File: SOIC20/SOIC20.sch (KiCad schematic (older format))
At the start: 5 parts, among them J1 Conn_01x10, J2 Conn_02x10_Counter_Clockwise, J3 Conn_02x10_Counter_Clockwise, J4 Conn_02x10_Counter_Clockwise, J5 Conn_01x10

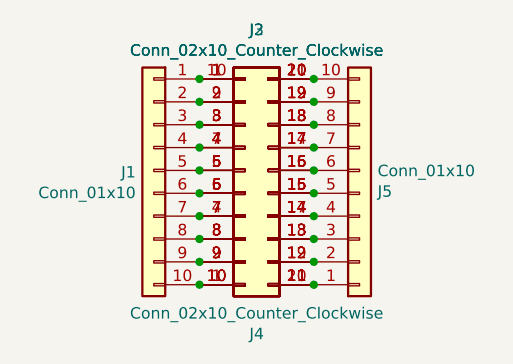
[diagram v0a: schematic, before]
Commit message: Silkscreens and sizes updated
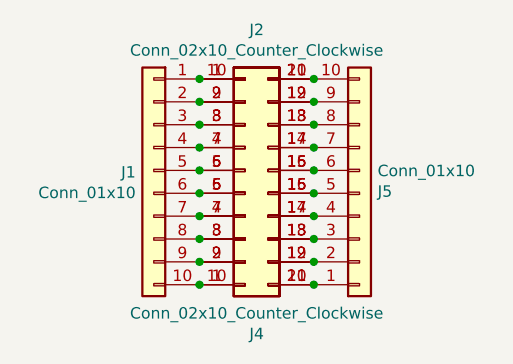
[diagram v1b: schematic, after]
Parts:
- removed J3: Conn_02x10_Counter_Clockwise, Package_DFN_QFN:QFN-20-1EP_5x5mm_P0.65mm_EP3.35x3.35mm, symbol Connector_Generic:Conn_02x10_Counter_Clockwise
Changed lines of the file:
@@
 EESchema Schematic File Version 4
+LIBS:SOIC20-cache
 EELAYER 29 0
 EELAYER END
@@
 	1    0    0    1
 $EndComp
-$Comp
-L Connector_Generic:Conn_02x10_Counter_Clockwise J3
-U 1 1 5D28B720
-P 4600 3700
-F 0 "J3" H 4650 4315 50  0000 C CNN
-F 1 "Conn_02x10_Counter_Clockwise" H 4650 4225 50  0000 C CNN
-F 2 "Package_DFN_QFN:QFN-20-1EP_5x5mm_P0.65mm_EP3.35x3.35mm" H 4600 3700 50  0001 C CNN
-F 3 "~" H 4600 3700 50  0001 C CNN
-	1    4600 3700
-	1    0    0    -1
-$EndComp
 Connection ~ 4400 3300

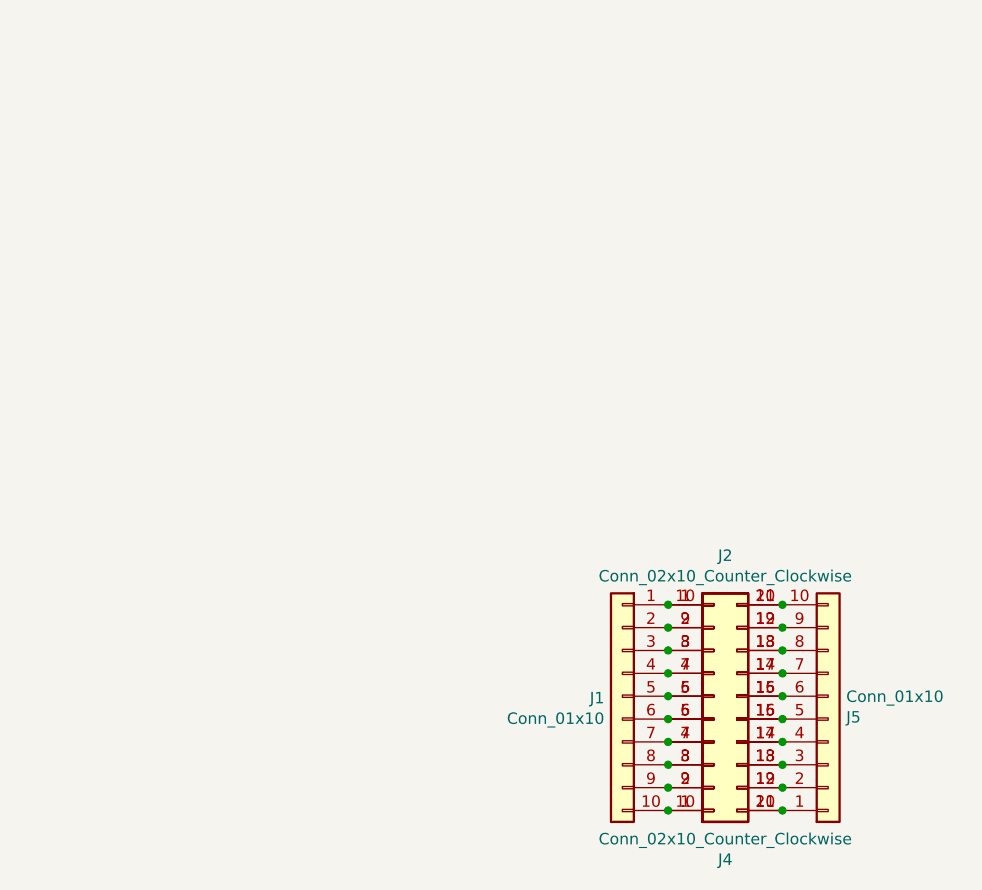
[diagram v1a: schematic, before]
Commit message: USB, SD and CR Cells Added
MicroSD, MicroUSB, MiniUSB, USB-C, CR1220, CR2032 added as well as all schematics page sizes optimised
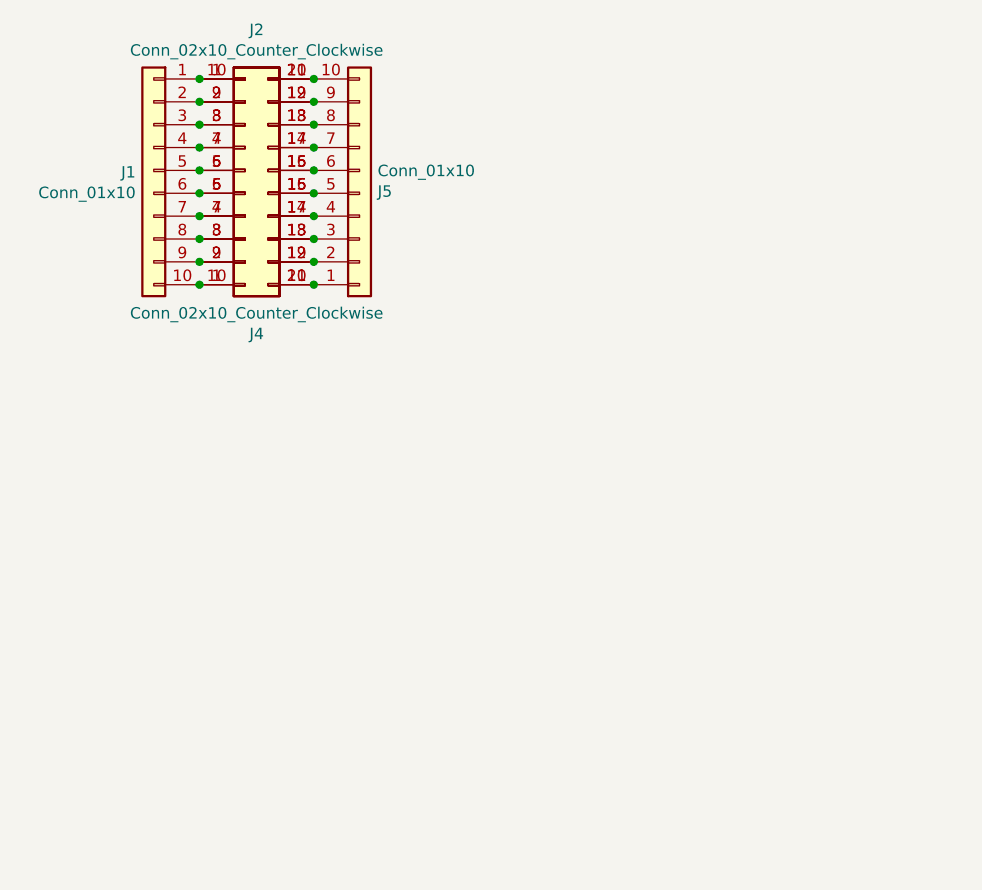
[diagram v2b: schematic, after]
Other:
- moved on the sheet: J1, J2, J4, J5
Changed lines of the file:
@@
 EELAYER 29 0
 EELAYER END
-$Descr A4 11693 8268
+$Descr User 5197 4016
 encoding utf-8
 Sheet 1 1
-Title ""
-Date ""
-Rev ""
-Comp ""
-Comment1 ""
-Comment2 ""
-Comment3 ""
+Title "SOIC20 To DIP20 Breakout Board"
+Date "2019-07-10"
+Rev "1"
+Comp "SirBoard"
+Comment1 "SOIC20 P = 1.27mm"
+Comment2 "TSSOP20 P = 0.65mm"
+Comment3 "DIP20 P = 2.54mm"
 Comment4 ""
 $EndDescr
@@
 L Connector_Generic:Conn_01x10 J5
 U 1 1 5D259BCE
-P 5100 3800
-F 0 "J5" H 5179 3792 50  0000 L CNN
-F 1 "Conn_01x10" H 5179 3702 50  0000 L CNN
-F 2 "Connector_PinHeader_2.54mm:PinHeader_1x10_P2.54mm_Vertical" H 5100 3800 50  0001 C CNN
-F 3 "~" H 5100 3800 50  0001 C CNN
-	1    5100 3800
+P 3050 1500
+F 0 "J5" H 3129 1492 50  0000 L CNN
+F 1 "Conn_01x10" H 3129 1402 50  0000 L CNN
+F 2 "Connector_PinHeader_2.54mm:PinHeader_1x10_P2.54mm_Vertical" H 3050 1500 50  0001 C CNN
+F 3 "~" H 3050 1500 50  0001 C CNN
+	1    3050 1500
 	1    0    0    1
 $EndComp
@@
 L Connector_Generic:Conn_01x10 J1
 U 1 1 5D25B9B9
-P 4200 3700
-F 0 "J1" H 4279 3692 50  0000 L CNN
-F 1 "Conn_01x10" H 4279 3602 50  0000 L CNN
-F 2 "Connector_PinHeader_2.54mm:PinHeader_1x10_P2.54mm_Vertical" H 4200 3700 50  0001 C CNN
-F 3 "~" H 4200 3700 50  0001 C CNN
-	1    4200 3700
+P 2150 1400
+F 0 "J1" H 2229 1392 50  0000 L CNN
+F 1 "Conn_01x10" H 2229 1302 50  0000 L CNN
+F 2 "Connector_PinHeader_2.54mm:PinHeader_1x10_P2.54mm_Vertical" H 2150 1400 50  0001 C CNN
+F 3 "~" H 2150 1400 50  0001 C CNN
+	1    2150 1400
 	-1   0    0    -1
 $EndComp
@@
 L Connector_Generic:Conn_02x10_Counter_Clockwise J2
 U 1 1 5D25A016
-P 4600 3700
-F 0 "J2" H 4650 4315 50  0000 C CNN
-F 1 "Conn_02x10_Counter_Clockwise" H 4650 4225 50  0000 C CNN
-F 2 "Package_SO:SOIC-20W_7.5x12.8mm_P1.27mm" H 4600 3700 50  0001 C CNN
-F 3 "~" H 4600 3700 50  0001 C CNN
-	1    4600 3700
+P 2550 1400
+F 0 "J2" H 2600 2015 50  0000 C CNN
+F 1 "Conn_02x10_Counter_Clockwise" H 2600 1925 50  0000 C CNN
+F 2 "Package_SO:SOIC-20W_7.5x12.8mm_P1.27mm" H 2550 1400 50  0001 C CNN
+F 3 "~" H 2550 1400 50  0001 C CNN
+	1    2550 1400
 	1    0    0    -1
 $EndComp
@@
 L Connector_Generic:Conn_02x10_Counter_Clockwise J4
 U 1 1 5D25E8E3
-P 4600 3800
-F 0 "J4" H 4650 4415 50  0000 C CNN
-F 1 "Conn_02x10_Counter_Clockwise" H 4650 4325 50  0000 C CNN
-F 2 "Package_SO:SSOP-20_4.4x6.5mm_P0.65mm" H 4600 3800 50  0001 C CNN
-F 3 "~" H 4600 3800 50  0001 C CNN
-	1    4600 3800
+P 2550 1500
+F 0 "J4" H 2600 2115 50  0000 C CNN
+F 1 "Conn_02x10_Counter_Clockwise" H 2600 2025 50  0000 C CNN
+F 2 "Package_SO:SSOP-20_4.4x6.5mm_P0.65mm" H 2550 1500 50  0001 C CNN
+F 3 "~" H 2550 1500 50  0001 C CNN
+	1    2550 1500
 	1    0    0    1
 $EndComp
-Connection ~ 4400 3300
-Connection ~ 4400 3400
-Connection ~ 4400 3500
-Connection ~ 4400 3600
-Connection ~ 4400 3700
-Connection ~ 4400 3800
-Connection ~ 4400 3900
-Connection ~ 4400 4000
-Connection ~ 4400 4100
-Connection ~ 4400 4200
-Connection ~ 4900 3300
-Connection ~ 4900 3400
-Connection ~ 4900 3500
-Connection ~ 4900 3600
-Connection ~ 4900 3700
-Connection ~ 4900 3800
-Connection ~ 4900 3900
-Connection ~ 4900 4000
-Connection ~ 4900 4100
-Connection ~ 4900 4200
+Connection ~ 2350 1000
+Connection ~ 2350 1100
+Connection ~ 2350 1200
+Connection ~ 2350 1300
+Connection ~ 2350 1400
+Connection ~ 2350 1500
+Connection ~ 2350 1600
+Connection ~ 2350 1700
+Connection ~ 2350 1800
+Connection ~ 2350 1900
+Connection ~ 2850 1000
+Connection ~ 2850 1100
+Connection ~ 2850 1200
+Connection ~ 2850 1300
+Connection ~ 2850 1400
+Connection ~ 2850 1500
+Connection ~ 2850 1600
+Connection ~ 2850 1700
+Connection ~ 2850 1800
+Connection ~ 2850 1900
 $EndSCHEMATC
